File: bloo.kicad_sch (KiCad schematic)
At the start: 94 parts, among them J5 SWD_Header, M1 M1_Conn_Alt, M2 M2_Conn_Alt, Q0 TEFT4300, Q1 TEFT4300, Q10 Q_NMOS_GSD, Q11 Q_NMOS_GSD, Q12 Q_NMOS_GSD, Q2 TEFT4300, Q3 TEFT4300, Q9 Q_NMOS_GSD, SW1 SW, SW2 SW, U1 YAAJ_BluePill_SWD_Breakout, U2 L293D, U3 LM1085-5.0, U4 NCP161ASN330T1G, U5 BC832, Y1 ABS07-32.768KHZ-T

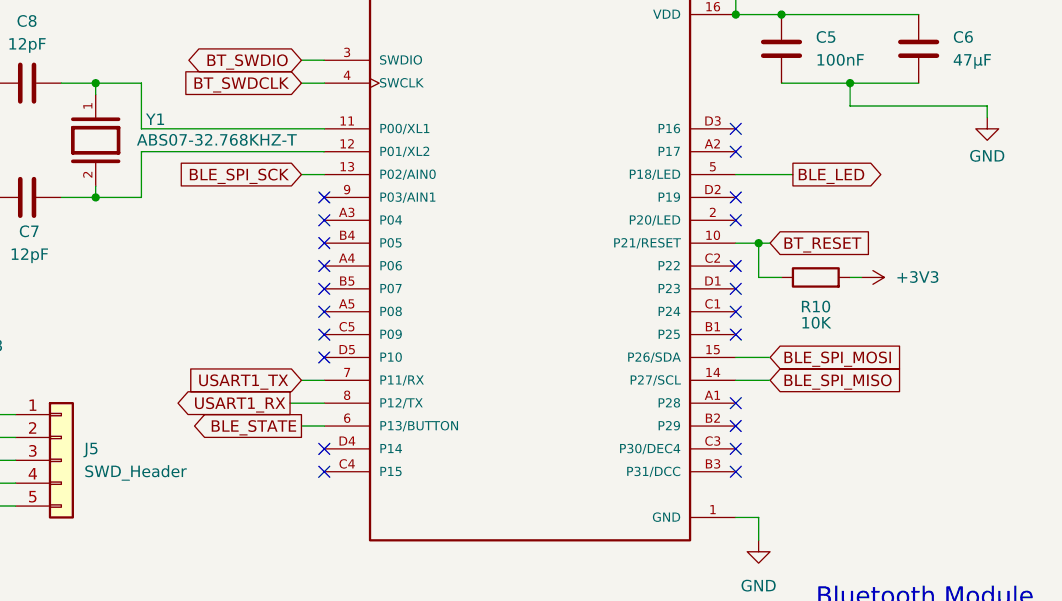
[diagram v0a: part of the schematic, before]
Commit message: updated correct jst battery connector
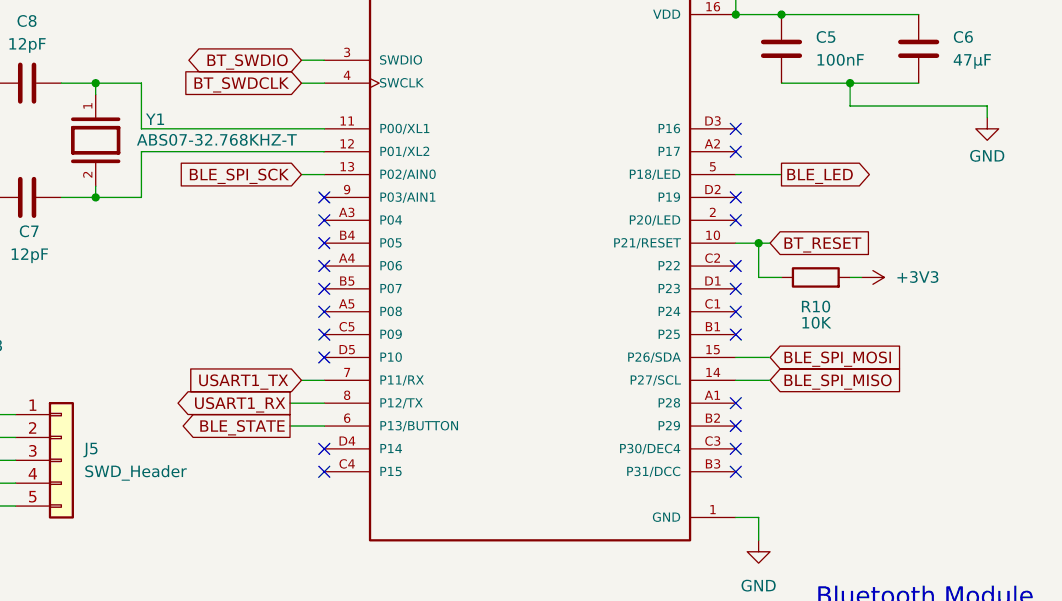
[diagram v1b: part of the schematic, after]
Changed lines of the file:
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@@
 	(wire
 		(pts
-			(xy 377.19 135.89) (xy 370.84 135.89)
+			(xy 375.92 135.89) (xy 370.84 135.89)
 		)
 		(stroke
@@
 	(wire
 		(pts
-			(xy 322.58 163.83) (xy 325.12 163.83)
+			(xy 321.31 163.83) (xy 325.12 163.83)
 		)
 		(stroke
@@
 	(global_label "BLE_LED"
 		(shape output)
-		(at 377.19 135.89 0)
+		(at 375.92 135.89 0)
 		(fields_autoplaced yes)
 		(effects
@@
 		)
 		(property "Intersheetrefs" "${INTERSHEET_REFS}"
-			(at 387.3828 135.89 0)
+			(at 386.1128 135.89 0)
 			(effects
 				(font
@@
 	(global_label "BLE_STATE"
 		(shape output)
-		(at 322.58 163.83 180)
+		(at 321.31 163.83 180)
 		(fields_autoplaced yes)
 		(effects
@@
 		)
 		(property "Intersheetrefs" "${INTERSHEET_REFS}"
-			(at 310.452 163.83 0)
+			(at 309.182 163.83 0)
 			(effects
 				(font

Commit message: updated DNP
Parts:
- D0, D1, D2, D3, Q0, Q1, Q2, Q3, U1, U5: now not fitted
- Y1: LCSC Part # (none) -> C130253
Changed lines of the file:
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@@
 		(in_bom yes)
 		(on_board yes)
-		(dnp no)
+		(dnp yes)
 		(property "Reference" "D3"
 			(at 101.5492 44.3484 90)
@@
 		(in_bom yes)
 		(on_board yes)
-		(dnp no)
+		(dnp yes)
 		(property "Reference" "Q0"
 			(at 40.8432 110.0074 0)
@@
 		(in_bom yes)
 		(on_board yes)
-		(dnp no)
+		(dnp yes)
 		(property "Reference" "Q1"
 			(at 59.2582 109.4994 0)
@@
 		(in_bom yes)
 		(on_board yes)
-		(dnp no)
+		(dnp yes)
 		(property "Reference" "Q2"
 			(at 108.5342 108.8644 0)
@@
 		(in_bom yes)
 		(on_board yes)
-		(dnp no)
+		(dnp yes)
 		(property "Reference" "Q3"
 			(at 84.9122 109.3724 0)
@@
 		(in_bom yes)
 		(on_board yes)
-		(dnp no)
+		(dnp yes)
 		(property "Reference" "D2"
 			(at 139.0142 44.7294 90)
@@
 		(in_bom yes)
 		(on_board yes)
-		(dnp no)
+		(dnp yes)
 		(property "Reference" "D0"
 			(at 28.0162 43.4594 90)
@@
 		(in_bom yes)
 		(on_board yes)
-		(dnp no)
+		(dnp yes)
 		(property "Reference" "D1"
 			(at 66.1162 43.4594 90)
@@
 			)
 		)
-		(property "Datasheet" "C2801245"
+		(property "Datasheet" ""
 			(at 388.62 212.09 0)
 			(effects
@@
 		(in_bom yes)
 		(on_board yes)
-		(dnp no)
+		(dnp yes)
 		(property "Reference" "U1"
 			(at 206.121 42.799 0)
@@
 			)
 		)
-		(property "Datasheet" "C2801245"
+		(property "Datasheet" ""
 			(at 303.53 204.47 0)
 			(effects
@@
 		(in_bom yes)
 		(on_board yes)
-		(dnp no)
+		(dnp yes)
 		(fields_autoplaced yes)
 		(property "Reference" "U5"
@@
 			)
 		)
-		(property "Datasheet" "C2801245"
+		(property "Datasheet" ""
 			(at 303.53 231.14 0)
 			(effects
@@
 				(hide yes)
 			)
+		)
+		(property "LCSC Part #" "C130253"
+			(at 299.72 132.08 90)
+			(effects
+				(font
+					(size 1.27 1.27)
+				)
+				(hide yes)
+			)

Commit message: switched to xt30 battery footprint
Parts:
- BT1: footprint Connector_JST:JST_EH_B2B-EH-A_1x02_P2.50mm_Vertical -> Connector_AMASS:AMASS_XT30UPB-M_1x02_P5.0mm_Vertical
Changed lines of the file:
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@@
 			)
 		)
-		(property "Footprint" "Connector_JST:JST_EH_B2B-EH-A_1x02_P2.50mm_Vertical"
+		(property "Footprint" "Connector_AMASS:AMASS_XT30UPB-M_1x02_P5.0mm_Vertical"
 			(at 30.48 238.506 90)
 			(effects

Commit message: updated BOM
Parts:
- BT1: LCSC Part # C160262 -> C99101
- BT_MH1, BT_MH2, BT_MH3, BT_MH4, J5, M_MH1, M_MH2, SK1, SK2, SK3, SK4, TP2, TP5, TP6: now not fitted
- C7, C8: LCSC Part # (none) -> C38523
- D7, D9: LCSC Part # (none) -> C516855
- R13, R14, R15, R16: value 47k -> 47K
- R23: LCSC Part # C2479751 -> C2479071
- R9: LCSC Part # C2479751 -> C25664
- SW1, SW2, SW_RST1: LCSC Part # C2801245 -> C778166
- U1: LCSC Part # C22396880 -> (none)
- U5: LCSC Part # C6470192 -> (none)
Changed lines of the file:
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@@
 			)
 		)
-		(property "Value" "47k"
+		(property "Value" "47K"
 			(at 101.6 71.9836 90)
 			(effects
@@
 			)
 		)
-		(property "Value" "47k"
+		(property "Value" "47K"
 			(at 139.065 72.3646 90)
 			(effects
@@
 			)
 		)
-		(property "Value" "47k"
+		(property "Value" "47K"
 			(at 28.067 71.0946 90)
 			(effects
@@
 			)
 		)
-		(property "Value" "47k"
+		(property "Value" "47K"
 			(at 66.167 71.0946 90)
 			(effects
@@
 		(in_bom yes)
 		(on_board yes)
-		(dnp no)
+		(dnp yes)
 		(property "Reference" "SK1"
 			(at 234.95 149.9616 0)
@@
 		(in_bom yes)
 		(on_board yes)
-		(dnp no)
+		(dnp yes)
 		(property "Reference" "BT_MH2"
 			(at 205.994 149.8346 0)
@@
 		(in_bom yes)
 		(on_board yes)
-		(dnp no)
+		(dnp yes)
 		(property "Reference" "BT_MH1"
 			(at 205.994 139.6746 0)
@@
 		(in_bom yes)
 		(on_board yes)
-		(dnp no)
+		(dnp yes)
 		(property "Reference" "SK2"
 			(at 234.95 140.4366 0)
@@
 			)
 		)
-		(property "LCSC Part #" "C160262 "
+		(property "LCSC Part #" "C99101"
 			(at 30.48 240.03 0)
 			(effects
@@
 			)
 		)
-		(property "LCSC Part #" "C2479751"
+		(property "LCSC Part #" "C2479071"
 			(at 52.07 251.46 0)
 			(effects
@@
 		(in_bom yes)
 		(on_board yes)
-		(dnp no)
+		(dnp yes)
 		(property "Reference" "SK3"
 			(at 245.745 140.4366 0)
@@
 		(in_bom yes)
 		(on_board yes)
-		(dnp no)
+		(dnp yes)
 		(property "Reference" "SK4"
 			(at 246.38 149.9616 0)
@@
 		(in_bom yes)
 		(on_board yes)
-		(dnp no)
+		(dnp yes)
 		(property "Reference" "TP2"
 			(at 101.8032 249.0978 0)
@@
 			)
 		)
-		(property "Datasheet" ""
+		(property "Datasheet" "https://tech.alpsalpine.com/cms.media/product_spec_skrpabe010_en_c1c577738a.pdf"
 			(at 388.62 212.09 0)
 			(effects
@@
 			)
 		)
-		(property "LCSC Part #" "C2801245"
+		(property "LCSC Part #" "C778166"
 			(at 388.62 217.17 0)
 			(effects
@@
 			)
 		)
-		(property "LCSC Part #" "C22396880"
+		(property "LCSC Part #" ""
 			(at 220.98 76.2 0)
 			(effects
@@
 		(in_bom yes)
 		(on_board yes)
-		(dnp no)
+		(dnp yes)
 		(property "Reference" "TP5"
 			(at 111.3282 249.0978 0)
@@
 		(in_bom yes)
 		(on_board yes)
-		(dnp no)
+		(dnp yes)
 		(property "Reference" "TP6"
 			(at 122.1232 249.0978 0)
@@
 		(in_bom yes)
 		(on_board yes)
-		(dnp no)
+		(dnp yes)
 		(property "Reference" "BT_MH4"
 			(at 192.913 150.2156 0)
@@
 		(in_bom yes)
 		(on_board yes)
-		(dnp no)
+		(dnp yes)
 		(property "Reference" "M_MH1"
 			(at 193.04 171.8056 0)
@@
 		(in_bom yes)
 		(on_board yes)
-		(dnp no)
+		(dnp yes)
 		(property "Reference" "M_MH2"
 			(at 205.486 171.8056 0)
@@
 			)
 		)
-		(property "Datasheet" ""
+		(property "Datasheet" "https://tech.alpsalpine.com/cms.media/product_spec_skrpabe010_en_c1c577738a.pdf"
 			(at 303.53 204.47 0)
 			(effects
@@
 			)
 		)
-		(property "LCSC Part #" "C2801245"
+		(property "LCSC Part #" "C778166"
 			(at 303.53 209.55 0)
 			(effects
@@
 		(in_bom yes)
 		(on_board yes)
-		(dnp no)
+		(dnp yes)
 		(property "Reference" "BT_MH3"
 			(at 192.913 140.0556 0)
@@
 			)
 		)
+		(property "LCSC Part #" "C38523"
+			(at 292.1 138.43 90)
+			(effects
+				(font
+					(size 1.27 1.27)
+				)
+				(hide yes)
+			)
+		)
 		(pin "1"
 		)
@@
 			)
 		)
+		(property "LCSC Part #" "C516855"
+			(at 365.76 217.17 0)
+			(effects
+				(font
+					(size 1.27 1.27)
+				)
+				(hide yes)
+			)
+		)
 		(pin "1"
 		)
@@
 			)
 		)
-		(property "LCSC Part #" "C6470192"
+		(property "LCSC Part #" ""
 			(at 347.98 146.05 0)
 			(effects
@@
 			)
 		)
+		(property "LCSC Part #" "C38523"
+			(at 292.1 125.73 90)
+			(effects
+				(font
+					(size 1.27 1.27)
+				)
+				(hide yes)
+			)
+		)
 		(pin "1"
 		)
@@
 			)
 		)
-		(property "Datasheet" ""
+		(property "Datasheet" "https://tech.alpsalpine.com/cms.media/product_spec_skrpabe010_en_c1c577738a.pdf"
 			(at 303.53 231.14 0)
 			(effects
@@
 			)
 		)
-		(property "LCSC Part #" "C2801245"
+		(property "LCSC Part #" "C778166"
 			(at 303.53 236.22 0)
 			(effects
@@
 			)
 		)
-		(property "LCSC Part #" "C2479751"
+		(property "LCSC Part #" "C25664"
 			(at 292.1 229.87 0)
 			(effects
@@
 		(in_bom yes)
 		(on_board yes)
-		(dnp no)
+		(dnp yes)
 		(property "Reference" "J5"
 			(at 298.45 166.3699 0)
@@
 			(at 365.76 222.25 0)
 			(effects
+				(font
+					(size 1.27 1.27)
+				)
+				(hide yes)
+			)
+		)
+		(property "LCSC Part #" "C516855"
+			(at 365.76 222.25 0)
+			(effects

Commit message: fix c6bom
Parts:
- C6: LCSC Part # C140782 -> C68361
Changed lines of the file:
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@@
 			)
 		)
-		(property "LCSC Part #" "C140782"
+		(property "LCSC Part #" "C68361"
 			(at 391.16 121.92 0)
 			(effects

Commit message: updated bom for out of stock component
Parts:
- C1, C12, C13, C19, C22, C4: LCSC Part # C600013 -> C1945
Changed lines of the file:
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@@
 			)
 		)
-		(property "LCSC Part #" "C600013"
+		(property "LCSC Part #" "C1945"
 			(at 162.56 238.76 0)
 			(effects
@@
 			)
 		)
-		(property "LCSC Part #" "C600013"
+		(property "LCSC Part #" "C1945"
 			(at 81.915 238.76 0)
 			(effects
@@
 			)
 		)
-		(property "LCSC Part #" "C600013"
+		(property "LCSC Part #" "C1945"
 			(at 109.22 188.595 0)
 			(effects
@@
 			)
 		)
-		(property "LCSC Part #" "C600013"
+		(property "LCSC Part #" "C1945"
 			(at 349.25 209.55 0)
 			(effects
@@
 			)
 		)
-		(property "LCSC Part #" "C600013"
+		(property "LCSC Part #" "C1945"
 			(at 349.25 228.6 0)
 			(effects
@@
 			)
 		)
-		(property "LCSC Part #" "C600013"
+		(property "LCSC Part #" "C1945"
 			(at 278.13 40.005 0)
 			(effects

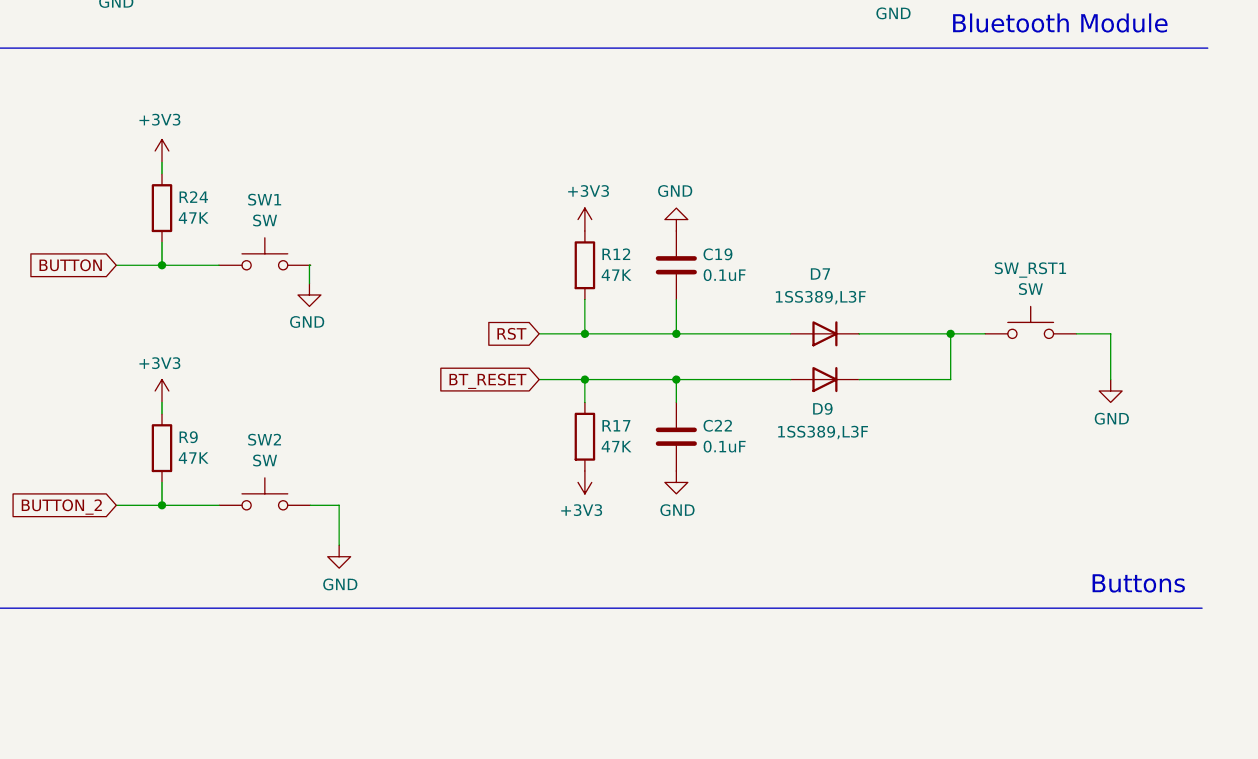
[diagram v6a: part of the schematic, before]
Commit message: fixed button symbol + rerouted
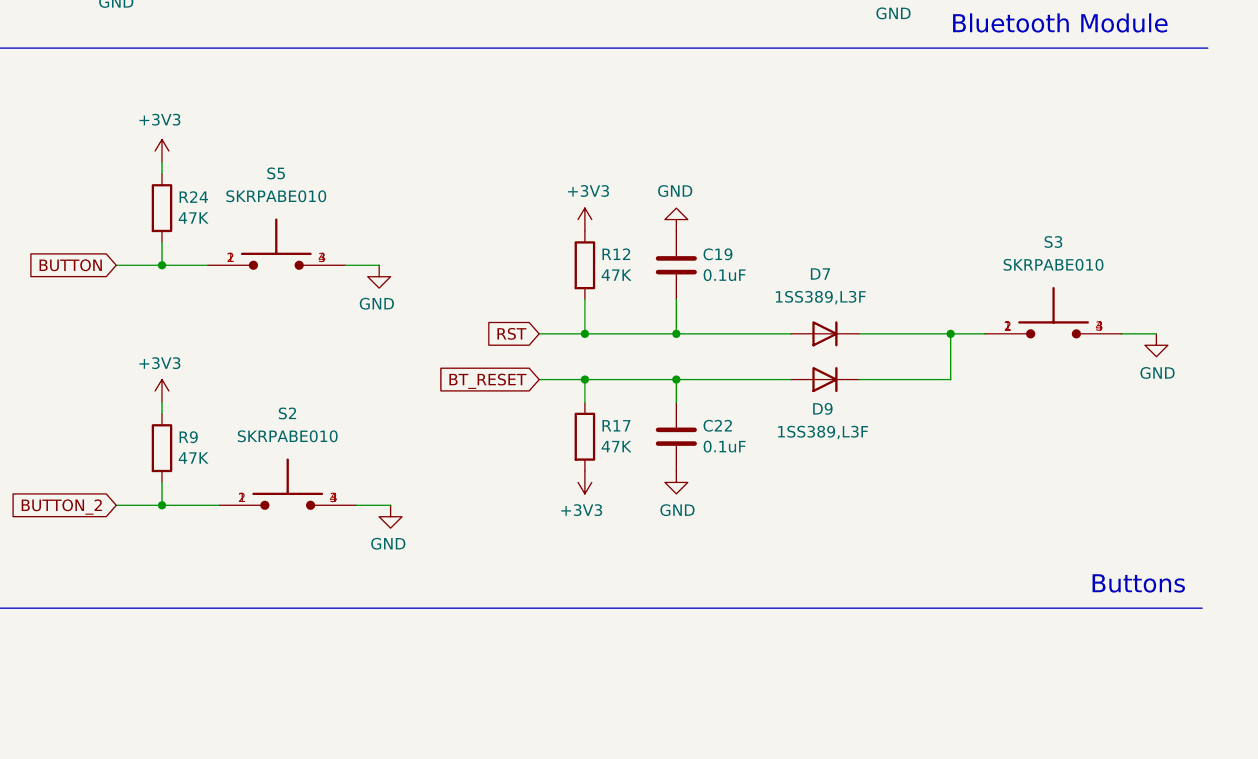
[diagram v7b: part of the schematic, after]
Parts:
- removed SW1, SW2, SW_RST1: SW, MM_Library:SW4_SKRPABE010_ALPS, symbol Switch:SW_Push
- added S2, S3, S5: SKRPABE010, MM_Library:SW4_SKRPABE010_ALPS, symbol BUTTON:SKRPABE010
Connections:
- net BUTTON: now also S5.1, S5.2
- net BUTTON_2: now also S2.1, S2.2
- net GND: now also S2.3, S2.4, S3.3, S3.4, S5.3, S5.4
- net at D7.1 (K), D9.1 (K): now also S3.1, S3.2
